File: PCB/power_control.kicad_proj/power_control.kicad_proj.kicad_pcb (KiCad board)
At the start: 2 copper layers, 70.5 x 64.5 mm, 14 parts, among them J7 ESP32_1, J8 ESP32_2

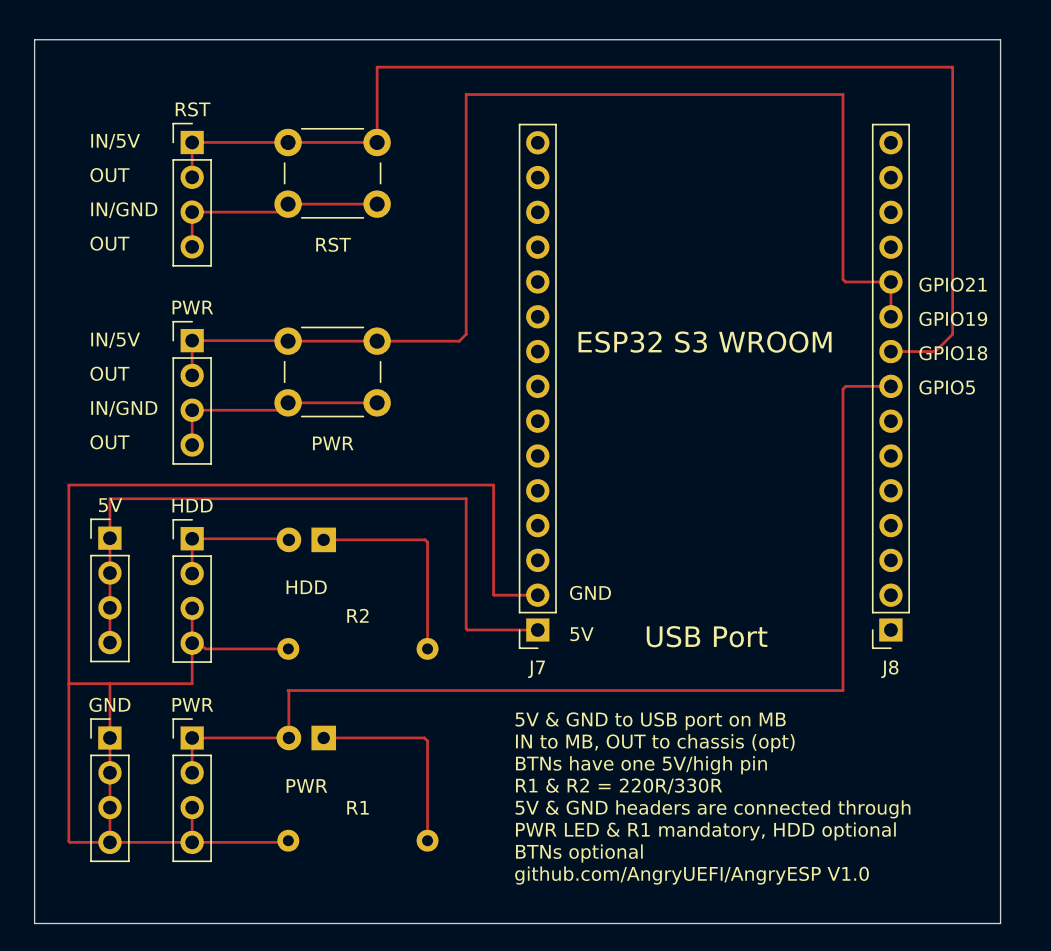
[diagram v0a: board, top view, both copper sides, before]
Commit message: PCB v1.1, adjust pin markings
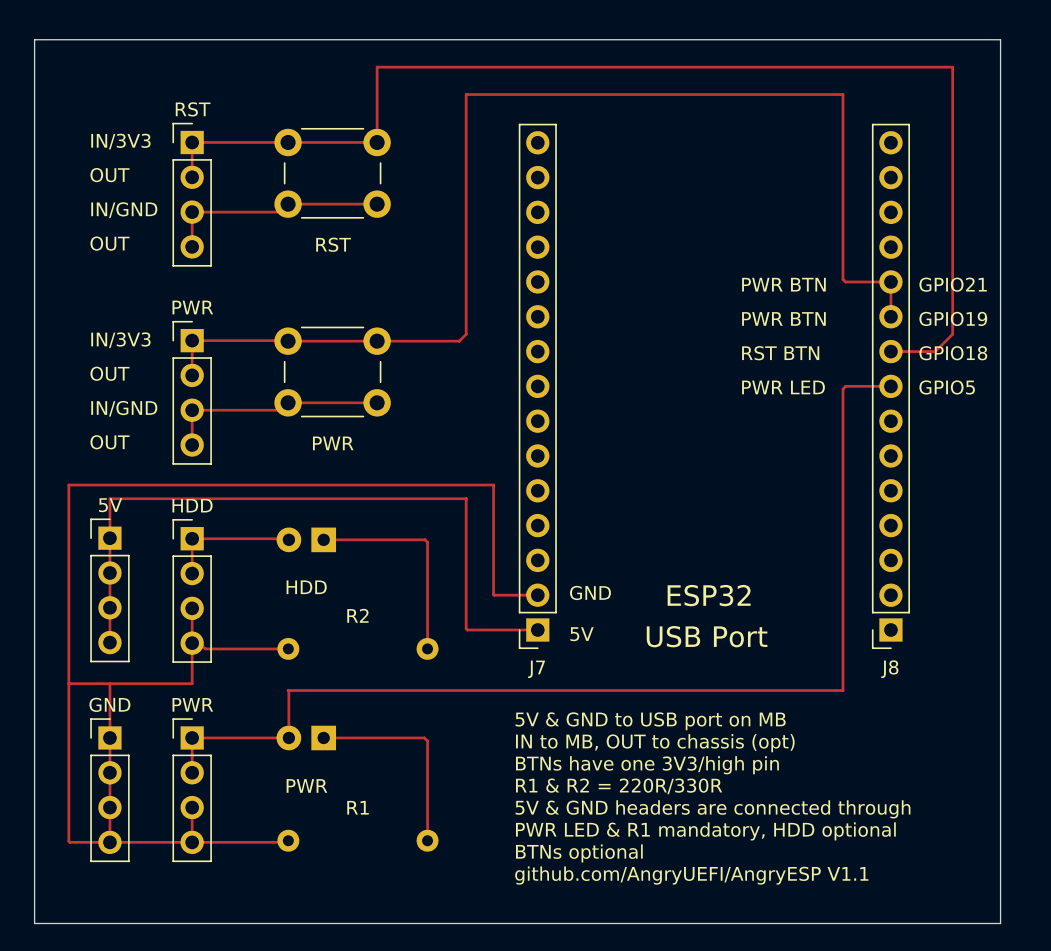
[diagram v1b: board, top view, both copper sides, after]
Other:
- board text added: "5V & GND to USB port on MB IN to MB, OUT to chassis (opt) BTNs have one 3V3/high pin R1 & R2 = 220R/330R 5V & GND headers are connected through PWR LED & R1 mandatory, HDD optional BTNs optional github.com/AngryUEFI/AngryESP V1.1"
- board text added: "ESP32"
- board text added: "IN/3V3"
- board text added: "PWR BTN"
- board text added: "PWR LED"
- board text added: "RST BTN"
- board text removed: "5V & GND to USB port on MB IN to MB, OUT to chassis (opt) BTNs have one 5V/high pin R1 & R2 = 220R/330R 5V & GND headers are connected through PWR LED & R1 mandatory, HDD optional BTNs optional github.com/AngryUEFI/AngryESP V1.0"
- board text removed: "ESP32 S3 WROOM"
- board text removed: "IN/5V"
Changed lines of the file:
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@@
 		(layer "Edge.Cuts")
+	)
+	(gr_text "RST BTN"
+		(at 90 62.5 0)
+		(layer "F.SilkS")
+		(effects
+			(font
+				(size 1 1)
+				(thickness 0.1)
+			)
+			(justify left bottom)
+		)
 	)
 	(gr_text "GPIO5"
@@
 		)
 	)
-	(gr_text "IN/5V"
+	(gr_text "PWR LED"
+		(at 90 65 0)
+		(layer "F.SilkS")
+		(effects
+			(font
+				(size 1 1)
+				(thickness 0.1)
+			)
+			(justify left bottom)
+		)
+	)
+	(gr_text "IN/3V3"
 		(at 42.5 61.5 0)
 		(layer "F.SilkS")
@@
 		)
 	)
-	(gr_text "ESP32 S3 WROOM"
-		(at 78 62 0)
+	(gr_text "ESP32"
+		(at 84.5 80.5 0)
 		(layer "F.SilkS")
 		(effects
@@
 		)
 	)
-	(gr_text "5V & GND to USB port on MB\nIN to MB, OUT to chassis (opt)\nBTNs have one 5V/high pin\nR1 & R2 = 220R/330R\n5V & GND headers are connected through\nPWR LED & R1 mandatory, HDD optional\nBTNs optional\ngithub.com/AngryUEFI/AngryESP V1.0"
+	(gr_text "5V & GND to USB port on MB\nIN to MB, OUT to chassis (opt)\nBTNs have one 3V3/high pin\nR1 & R2 = 220R/330R\n5V & GND headers are connected through\nPWR LED & R1 mandatory, HDD optional\nBTNs optional\ngithub.com/AngryUEFI/AngryESP V1.1"
 		(at 73.5 100.5 0)
 		(layer "F.SilkS")
@@
 		)
 	)
-	(gr_text "IN/5V"
+	(gr_text "IN/3V3"
 		(at 42.5 47 0)
 		(layer "F.SilkS")
@@
 		)
 	)
+	(gr_text "PWR BTN"
+		(at 90 57.5 0)
+		(layer "F.SilkS")
+		(effects
+			(font
+				(size 1 1)
+				(thickness 0.1)
+			)
+			(justify left bottom)
+		)
+	)
 	(gr_text "USB Port"
 		(at 83 83.5 0)
@@
 			)
 			(justify left bottom)
+		)
+	)
+	(gr_text "PWR BTN"
+		(at 90 60 0)
+		(layer "F.SilkS")
+		(effects
+			(font
+				(size 1 1)
+				(thickness 0.1)
+			)
+			(justify left bottom)

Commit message: Major rework of PCB, incompatible!
use transistors to sense LED and switch pins
add system header compatible with mainboard header
move pins to one side -> only single header required
we now need two PCB sides, yay
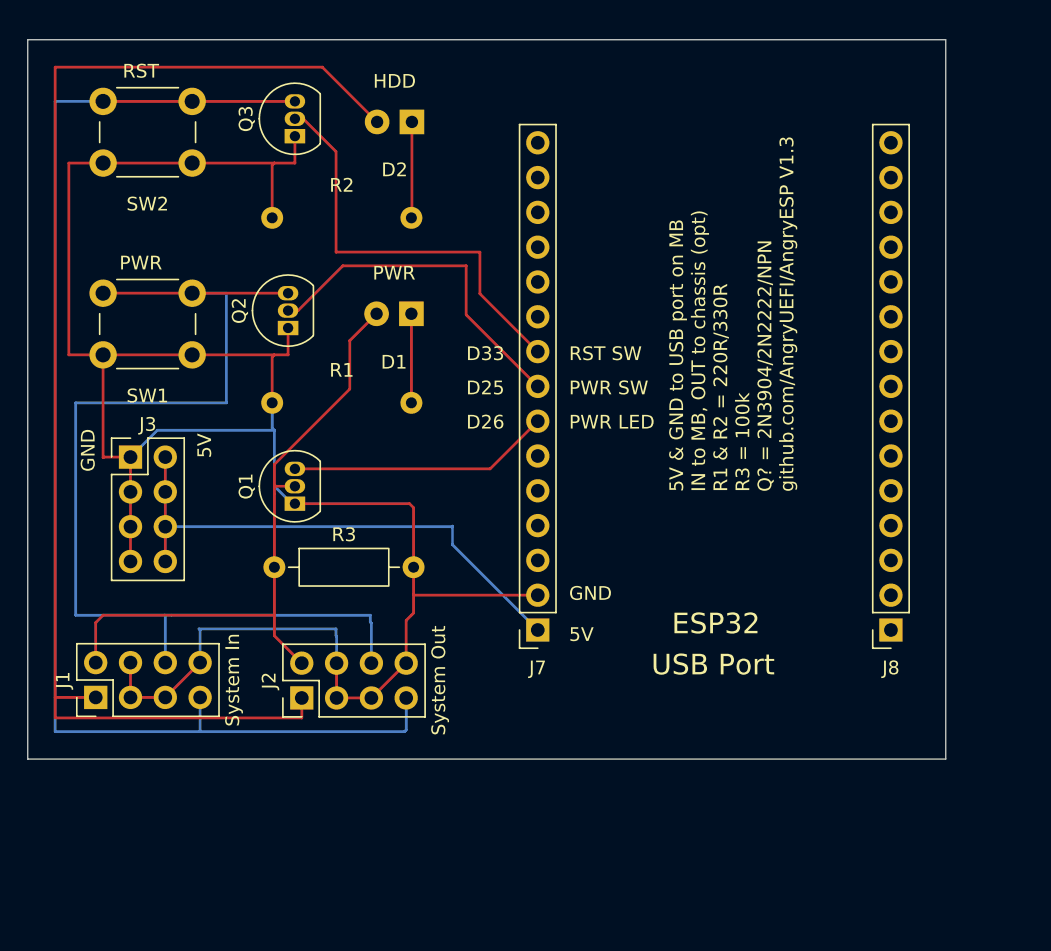
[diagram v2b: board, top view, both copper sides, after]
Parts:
- removed 5V: 5V, Connector_PinHeader_2.54mm:PinHeader_1x04_P2.54mm_Vertical
- removed GND: GND, Connector_PinHeader_2.54mm:PinHeader_1x04_P2.54mm_Vertical
- removed HDD: HDD LED, Connector_PinHeader_2.54mm:PinHeader_1x04_P2.54mm_Vertical
- removed PWR: PWR SW, Connector_PinHeader_2.54mm:PinHeader_1x04_P2.54mm_Vertical
- removed PWR: PWR LED, Connector_PinHeader_2.54mm:PinHeader_1x04_P2.54mm_Vertical
- removed RST: RST SW, Connector_PinHeader_2.54mm:PinHeader_1x04_P2.54mm_Vertical
- added J1: System In, Connector_PinHeader_2.54mm:PinHeader_2x04_P2.54mm_Vertical, F.Cu at (43.0, 87.0)
- added J2: System Out, Connector_PinHeader_2.54mm:PinHeader_2x04_P2.54mm_Vertical, F.Cu at (58.0, 87.0)
- added J3: Aux PWR, Connector_PinHeader_2.54mm:PinHeader_2x04_P2.54mm_Vertical, F.Cu at (45.5, 69.5)
- added Q1: 2N3904, Package_TO_SOT_THT:TO-92_Inline, F.Cu at (57.5, 72.9)
- added Q2: 2N3904, Package_TO_SOT_THT:TO-92_Inline, F.Cu at (57.0, 60.0)
- added Q3: 2N3904, Package_TO_SOT_THT:TO-92_Inline, F.Cu at (57.5, 46.0)
- added R3: 100k, Resistor_THT:R_Axial_DIN0207_L6.3mm_D2.5mm_P10.16mm_Horizontal, F.Cu at (56.0, 77.5)
- moved R1 32.0 mm to (55.8, 65.5)
- moved D1 31.6 mm to (66.0, 59.0)
- moved R2 31.5 mm to (55.8, 52.0)
- moved D2 31.2 mm to (66.0, 45.0)
- moved SW1 13.9 mm to (50.0, 62.0)
- moved SW2 13.8 mm to (50.0, 48.0)
- renumbered PWR to D1, HDD to D2, PWR to SW1, RST to SW2
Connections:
- J7 pad 7: unconnected-(J7-Pin_7-Pad7) -> Net-(J7-D26)
- J7 pad 8: unconnected-(J7-Pin_8-Pad8) -> Net-(J7-D25)
- J7 pad 9: unconnected-(J7-Pin_9-Pad9) -> Net-(J7-D33)
- J8 pad 10: Net-(J5-Pin_1) -> unconnected-(J8-Pin_10-Pad10)
- J8 pad 11: Net-(J5-Pin_1) -> unconnected-(J8-Pin_11-Pad11)
- J8 pad 8: Net-(D1-A) -> unconnected-(J8-Pin_8-Pad8)
- J8 pad 9: Net-(J6-Pin_1) -> unconnected-(J8-Pin_9-Pad9)
- SW1 pad 1: Net-(J5-Pin_3) -> GND
- SW1 pad 2: Net-(J5-Pin_1) -> Net-(J1-PWR_BTN+)
- SW2 pad 1: Net-(J6-Pin_3) -> GND
- SW2 pad 2: Net-(J6-Pin_1) -> Net-(J1-RST+)
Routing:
- net Net-(J1-RST+): track 0.00 -> 94.0 mm
- net Net-(J6-Pin_1): track 88.1 -> 0.00 mm
- net Net-(J5-Pin_1): track 87.4 -> 0.00 mm
- net Net-(D2-A): track 9.63 -> 95.1 mm
- net Net-(J1-PWR_BTN+): track 0.00 -> 79.0 mm
- net GND: track 120.2 -> 156.5 mm
- net Net-(D1-A): track 79.2 -> 47.1 mm
- net Net-(J7-D33): track 0.00 -> 30.8 mm
- net Net-(J7-D25): track 0.00 -> 25.3 mm
- net Net-(J7-D26): track 0.00 -> 19.2 mm
- net Net-(J6-Pin_3): track 16.3 -> 0.00 mm
- net Net-(J5-Pin_3): track 16.3 -> 0.00 mm
- net +5V: track 51.3 -> 38.8 mm
- net Net-(D1-K): track 15.0 -> 6.50 mm
- net Net-(D2-K): track 15.4 -> 7.02 mm
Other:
- board size 70.5 x 64.5 mm -> 67 x 52.5 mm
- board text added: "5V & GND to USB port on MB IN to MB, OUT to chassis (opt) R1 & R2 = 220R/330R R3 = 100k Q? = 2N3904/2N2222/NPN github.com/AngryUEFI/AngryESP V1.3"
- board text added: "D25"
- board text added: "D26"
- board text added: "D33"
- board text added: "PWR SW"
- board text added: "RST SW"
- board text removed: "5V & GND to USB port on MB IN to MB, OUT to chassis (opt) BTNs have one 3V3/high pin R1 & R2 = 220R/330R 5V & GND headers are connected through PWR LED & R1 mandatory, HDD optional BTNs optional github.com/AngryUEFI/AngryESP V1.1"
- board text removed: "GPIO18"
- board text removed: "GPIO19"
- board text removed: "GPIO21"
- board text removed: "GPIO5"
- board text removed: "IN/3V3"
- board text removed: "IN/GND"
- board text removed: "OUT"
- board text removed: "PWR BTN"
- board text removed: "RST BTN"
